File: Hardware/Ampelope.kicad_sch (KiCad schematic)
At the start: 17 parts, among them J1 Gate1_In, J3 Eurorack_10_pin_power, J4 RM_OUT, U1 TL074

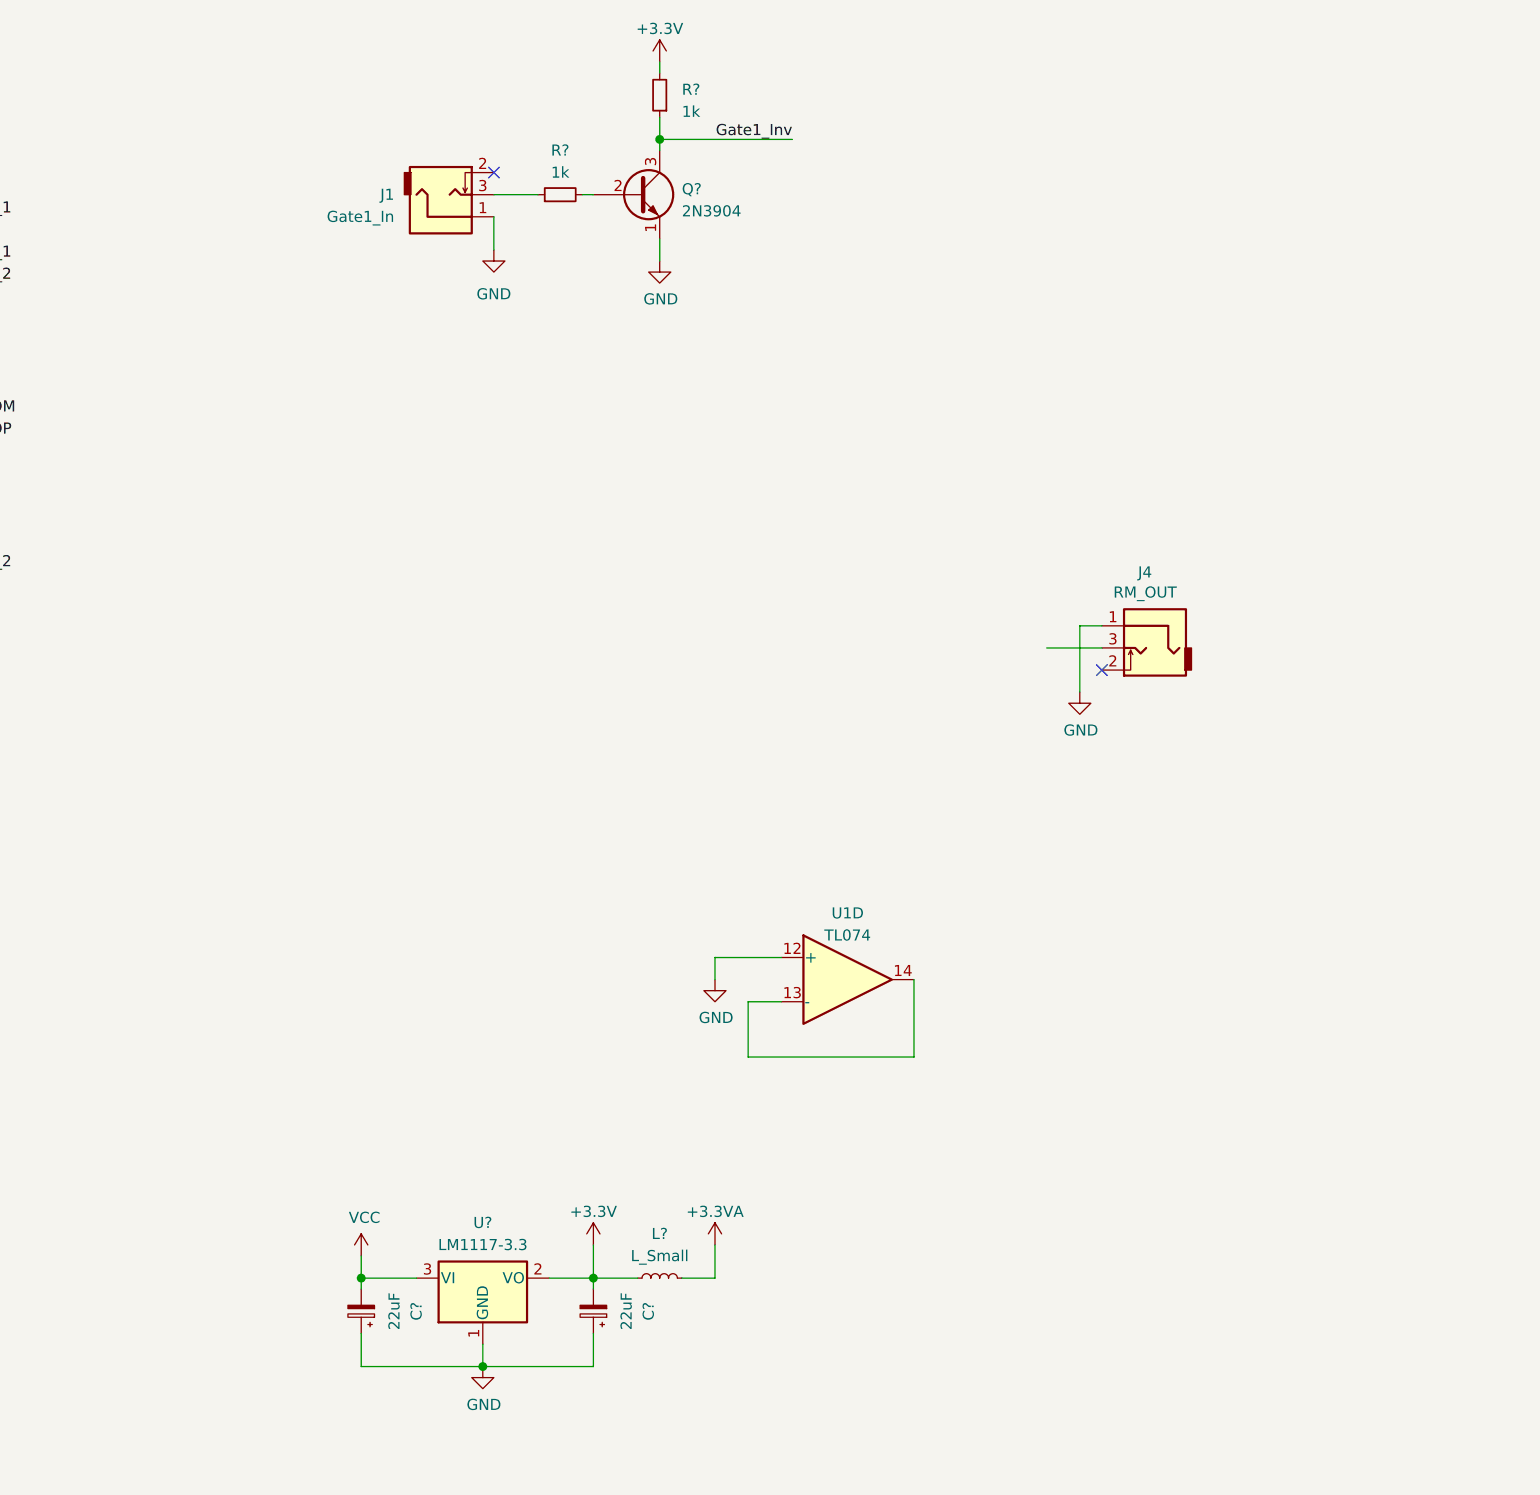
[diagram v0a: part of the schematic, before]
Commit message: Envelope 1 with VCA working; schematic updated
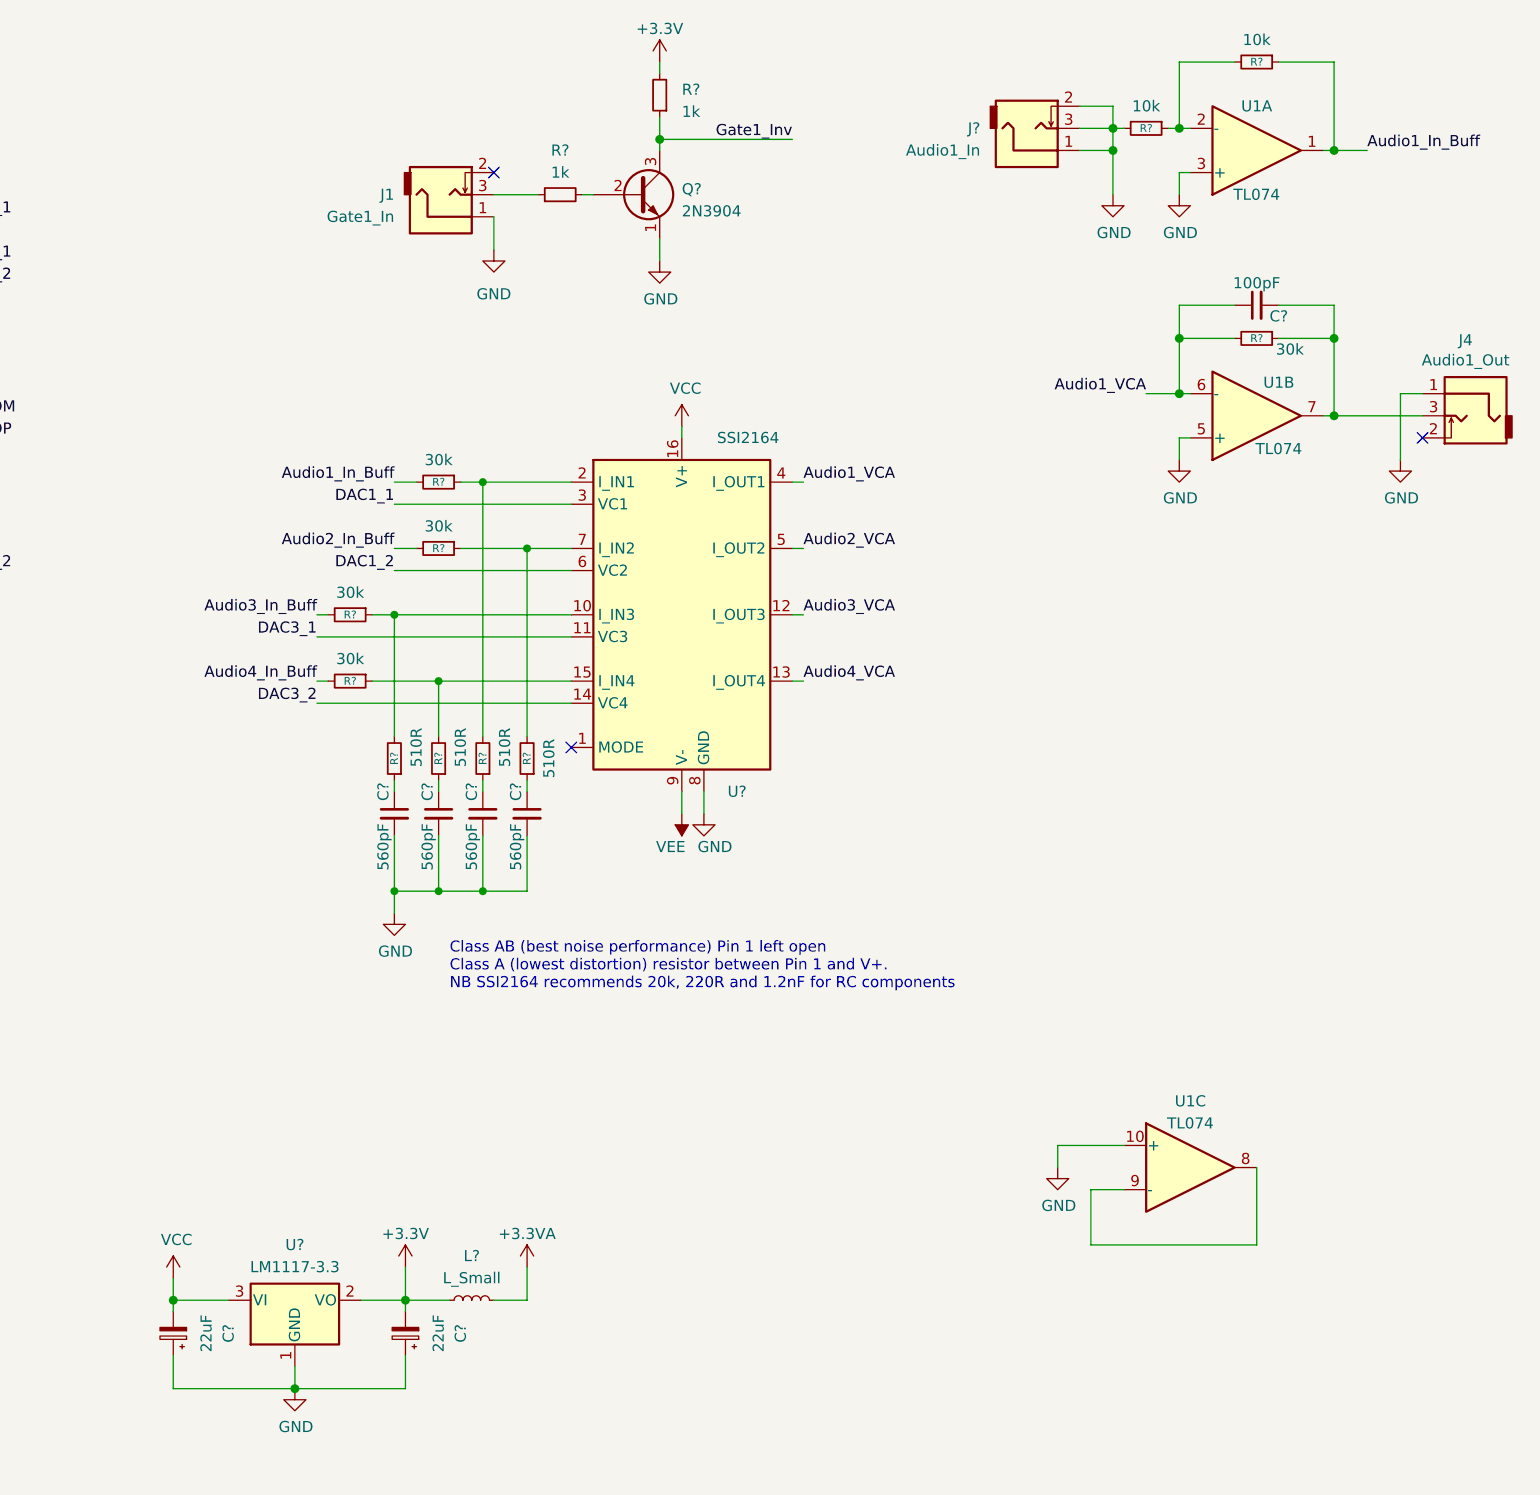
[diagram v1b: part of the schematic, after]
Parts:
- added C? (x4): 560pF, Capacitors_SMD:C_0603_HandSoldering, symbol Device:C_Small
- added C?: 100pF, symbol Device:C_Small
- added J?: Audio1_In, symbol thonkiconn:AudioJack2_Ground_Switch
- added R? (x4): 510R, Resistors_SMD:R_0603_HandSoldering, symbol Device:R_Small
- added R? (x5): 30k, Resistors_SMD:R_0603_HandSoldering, symbol Device:R_Small
- added R? (x2): 10k, Resistors_SMD:R_0603_HandSoldering, symbol Device:R_Small
- added unit 1 of U1
- added unit 2 of U1
- added U?: SSI2164, Package_SO:SOIC-16_3.9x9.9mm_P1.27mm, symbol Audio:SSI2164
- J4: value RM_OUT -> Audio1_Out
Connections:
- net DAC1_1: now also U?.3 (VC1)
- net DAC1_2: now also U?.6 (VC2)
- net DAC3_1: now also U?.11 (VC3)
- net DAC3_2: now also U?.14 (VC4)
- net GND: now also U1.10 (+), C?.2, C?.2, C?.2, C?.2, J?.1, J?.2, J?.3, R?.2, U1.3 (+), U1.5 (+), U?.8 (GND); no longer U1.12 (+)
- net VCC: now also U?.16 (V+)
- net VEE: now also U?.9 (V-)
- net at J4.3: now also C?.2, R?.1, U1.7
- new net: C?.1, R?.1 (x4)
- new net: R?.1, R?.2, U?.7 (I_IN2)
- new net: R?.1, R?.2, U?.15 (I_IN4)
- new net: R?.1, R?.2, U?.10 (I_IN3)
- new net: R?.1, R?.2, U?.2 (I_IN1)
- new net: R?.1, R?.2, U1.2 (-)
- new net: U1.8, U1.9 (-)
- new net Audio1_In_Buff: R?.1, R?.2, U1.1
- new net Audio1_VCA: C?.1, R?.2, U1.6 (-), U?.4 (I_OUT1)
- new net Audio2_In_Buff: R?.2
- new net Audio2_VCA: U?.5 (I_OUT2)
- new net Audio3_In_Buff: R?.2
- new net Audio3_VCA: U?.12 (I_OUT3)
- new net Audio4_In_Buff: R?.2
- new net Audio4_VCA: U?.13 (I_OUT4)
- no-connect marks 2 -> 3
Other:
- note added: "Class AB (best noise performance) Pin 1 left open Class A (lowest distortion) resistor between Pin 1 and V+. NB SSI2164 recommends 20k, 220R and 1.2nF for RC components"
- moved on the sheet: C?, J4, L?, U1C, U?

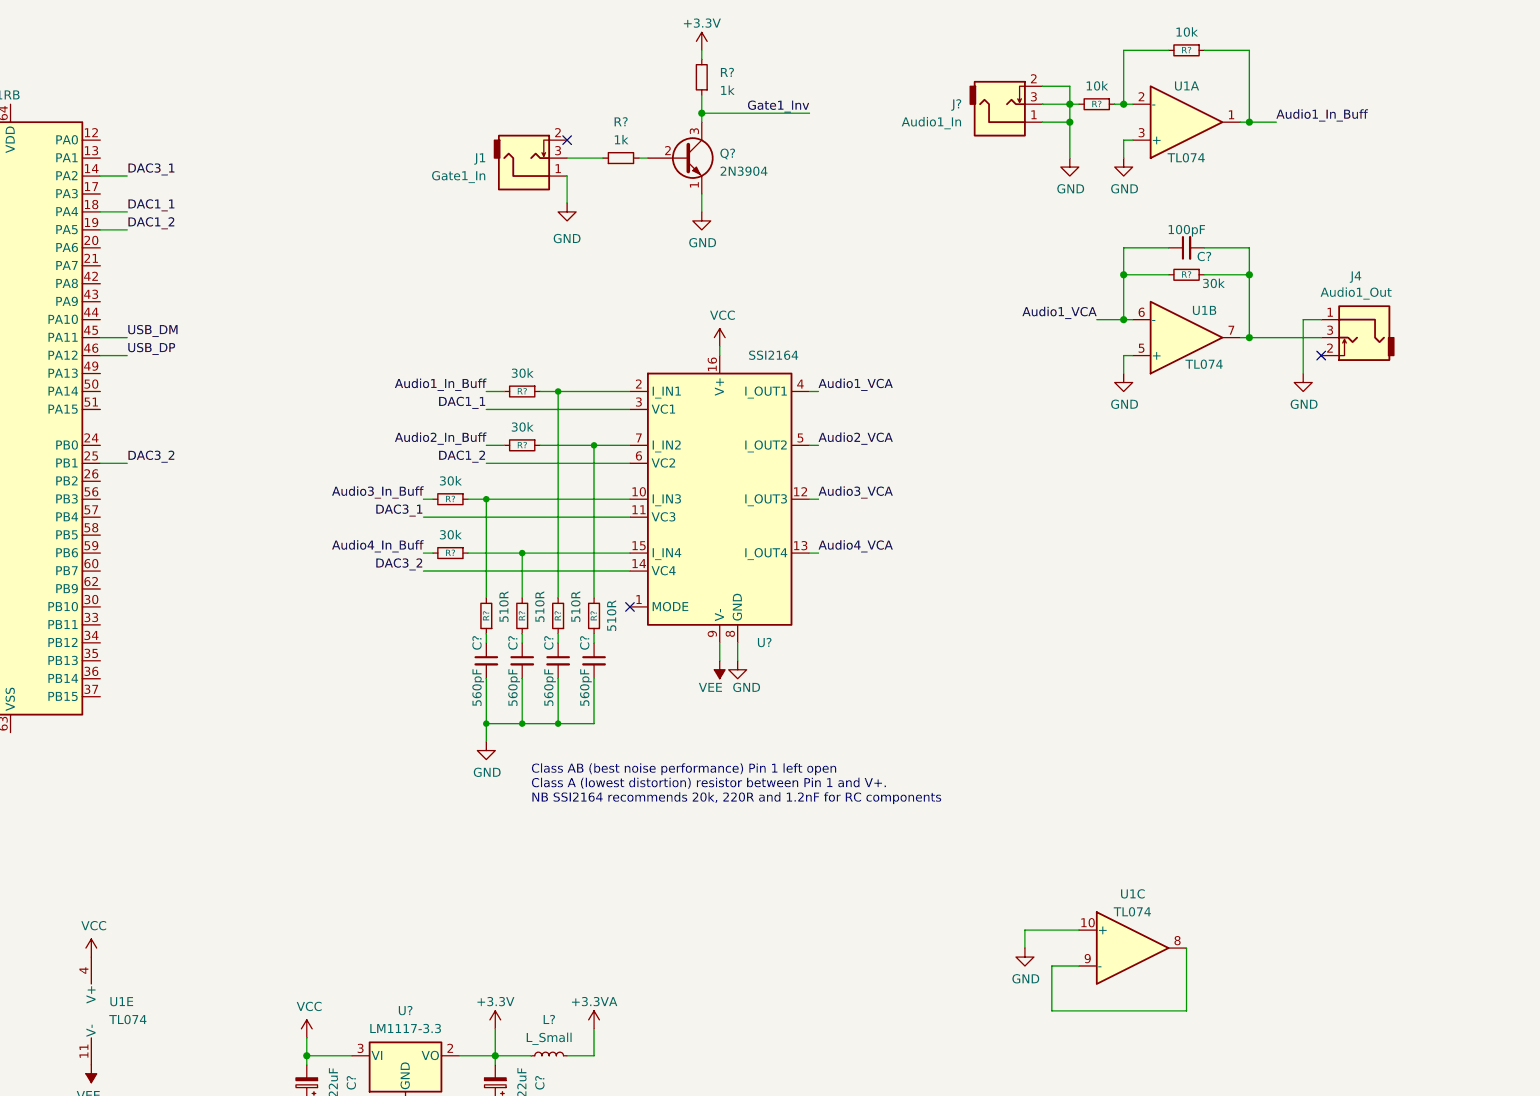
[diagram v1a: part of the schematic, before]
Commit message: More CORDIC tests; schematic updates
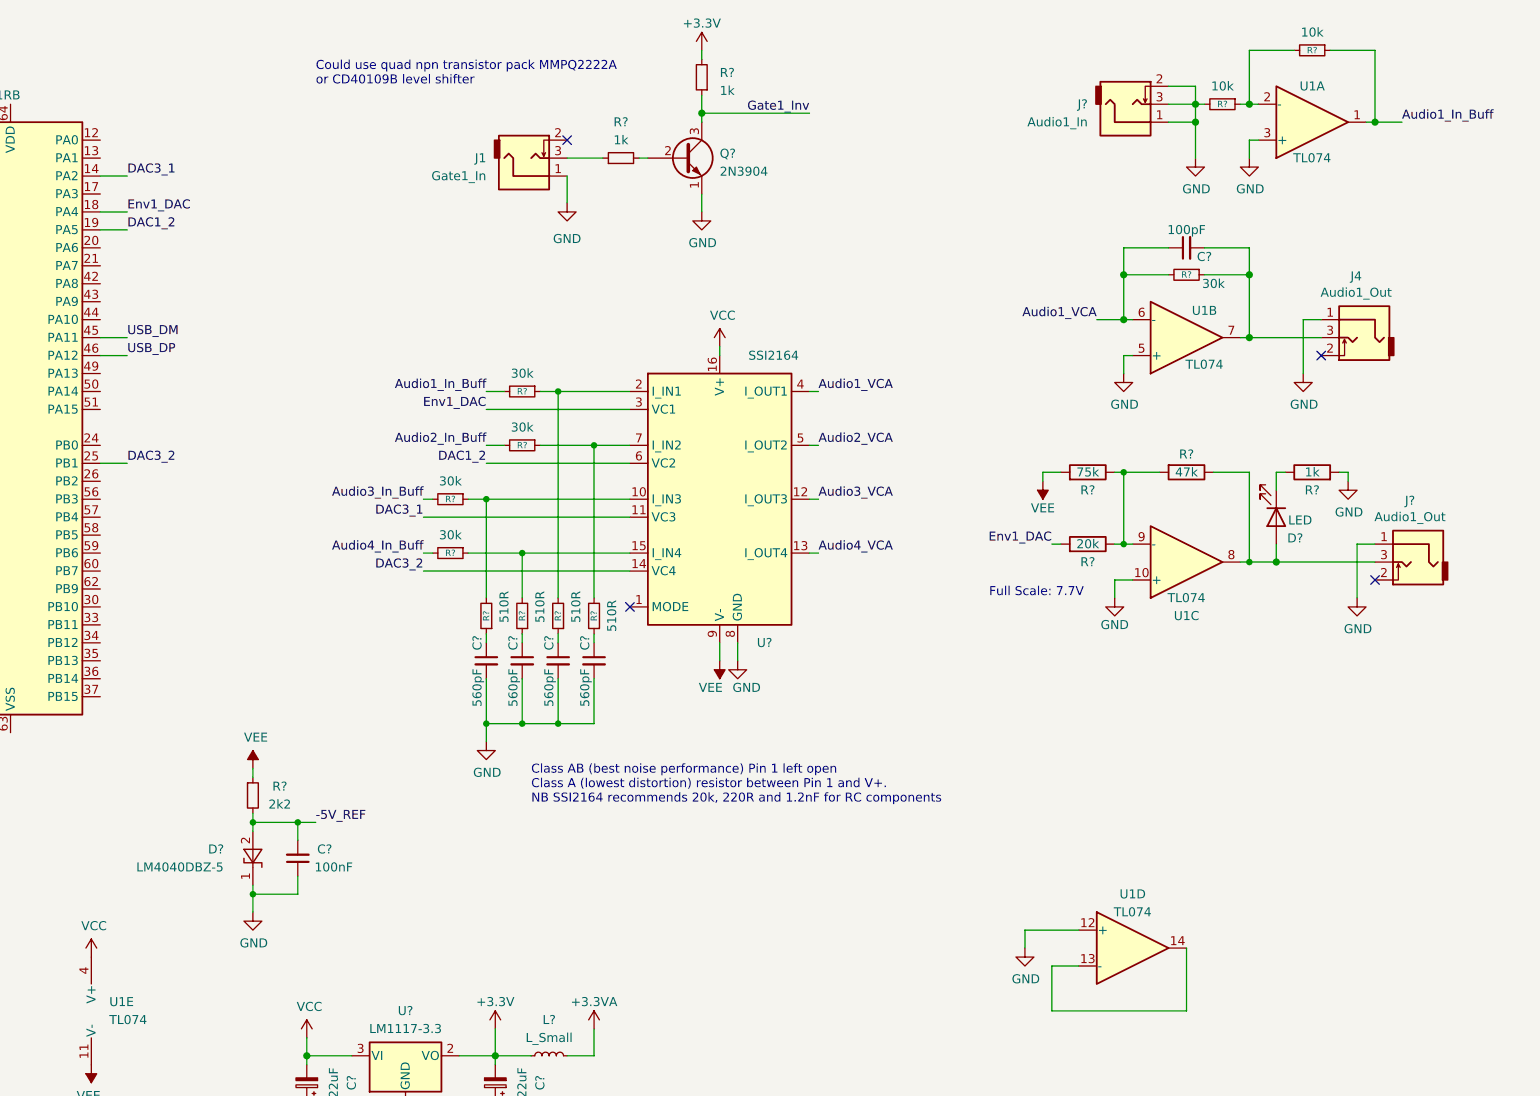
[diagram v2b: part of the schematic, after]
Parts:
- added C?: 100nF, Capacitors_SMD:C_0603_HandSoldering, symbol Device:C_Small
- added D?: LM4040DBZ-5, TO_SOT_Packages_SMD:SOT-23, symbol Reference_Voltage:LM4040DBZ-10
- added D?: LED, symbol Device:LED
- added J?: Audio1_Out, Custom_Footprints:THONKICONN_hole, symbol thonkiconn:AudioJack2_Ground_Switch
- added R?: 2k2, Resistors_SMD:R_0603_HandSoldering, symbol Device:R_Small
- added R?: 20k, Resistors_SMD:R_0603_HandSoldering, symbol Device:R
- added R?: 75k, Resistors_SMD:R_0603_HandSoldering, symbol Device:R
- added R?: 1k, Resistors_SMD:R_0603_HandSoldering, symbol Device:R
- added R?: 47k, Resistors_SMD:R_0603_HandSoldering, symbol Device:R
- added unit 3 of U1
- J1, J?: footprint (none) -> Custom_Footprints:THONKICONN_hole
- R? (x3): footprint (none) -> Resistors_SMD:R_0603_HandSoldering
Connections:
- net GND: now also U1.12 (+), C?.1, D?.1 (K), J?.1, R?.2, U1.10 (+); no longer U1.10 (+)
- net VEE: now also R?.1, R?.2
- net DAC1_1 renamed Env1_DAC
- net Env1_DAC: now also R?.2
- new net: D?.2 (A), J?.3, R?.1, U1.8
- new net: R?.1, R?.1, R?.2, U1.9 (-)
- new net: U1.13 (-), U1.14
- new net: D?.1 (K), R?.1
- new net -5V_REF: C?.2, D?.2 (A), R?.2
- no-connect marks 3 -> 4
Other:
- note added: "Could use quad npn transistor pack MMPQ2222A or CD40109B level shifter"
- note added: "Full Scale: 7.7V"
- moved on the sheet: J?, R?, U1A
